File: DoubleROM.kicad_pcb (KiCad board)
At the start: 2 copper layers, 81.3 x 53.6 mm, 19 parts, among them J1 Bus_ISA_8bit, SW1 ROM 1 Config, SW2 ROM 2 Config, SW3 Size, SW4 Size, U1 ROM 1, U2 ROM 2, U3 74LS688, U4 74LS688, U5 74LS33

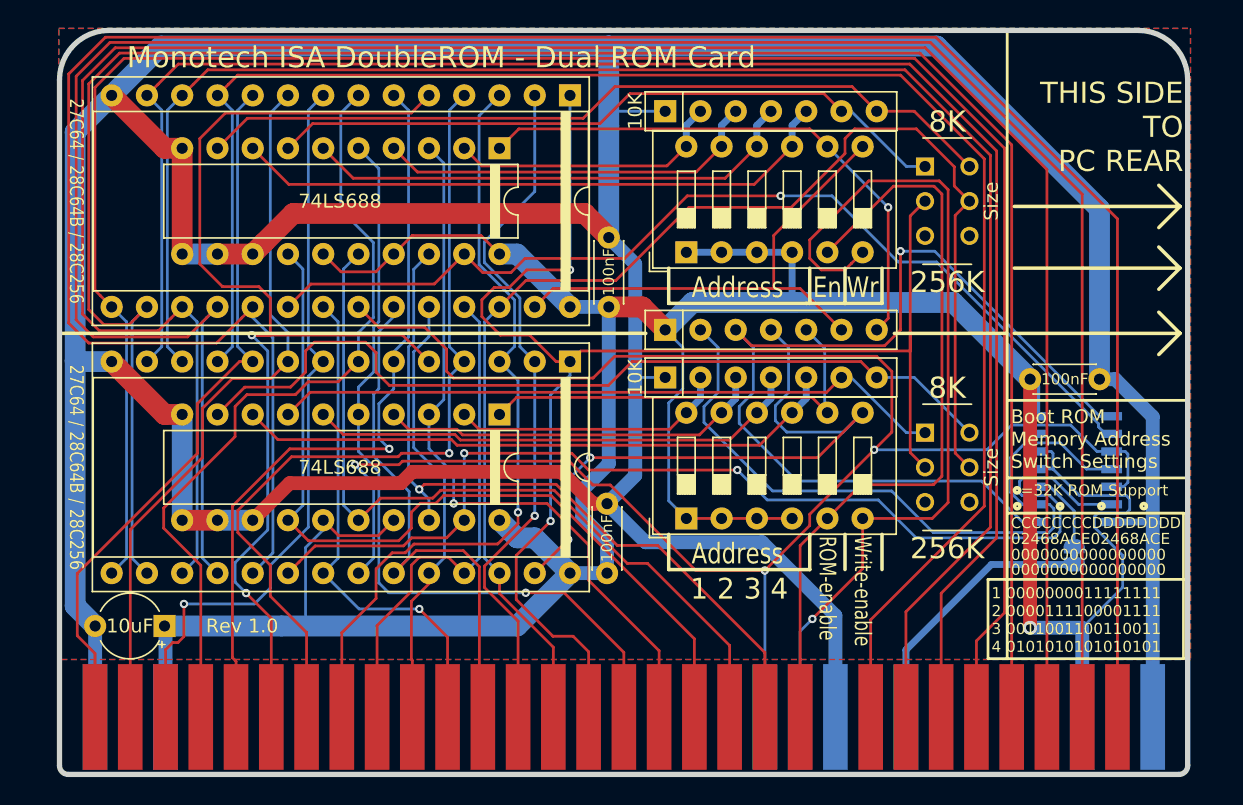
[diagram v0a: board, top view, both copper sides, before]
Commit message: minor change in text 256K to 32K
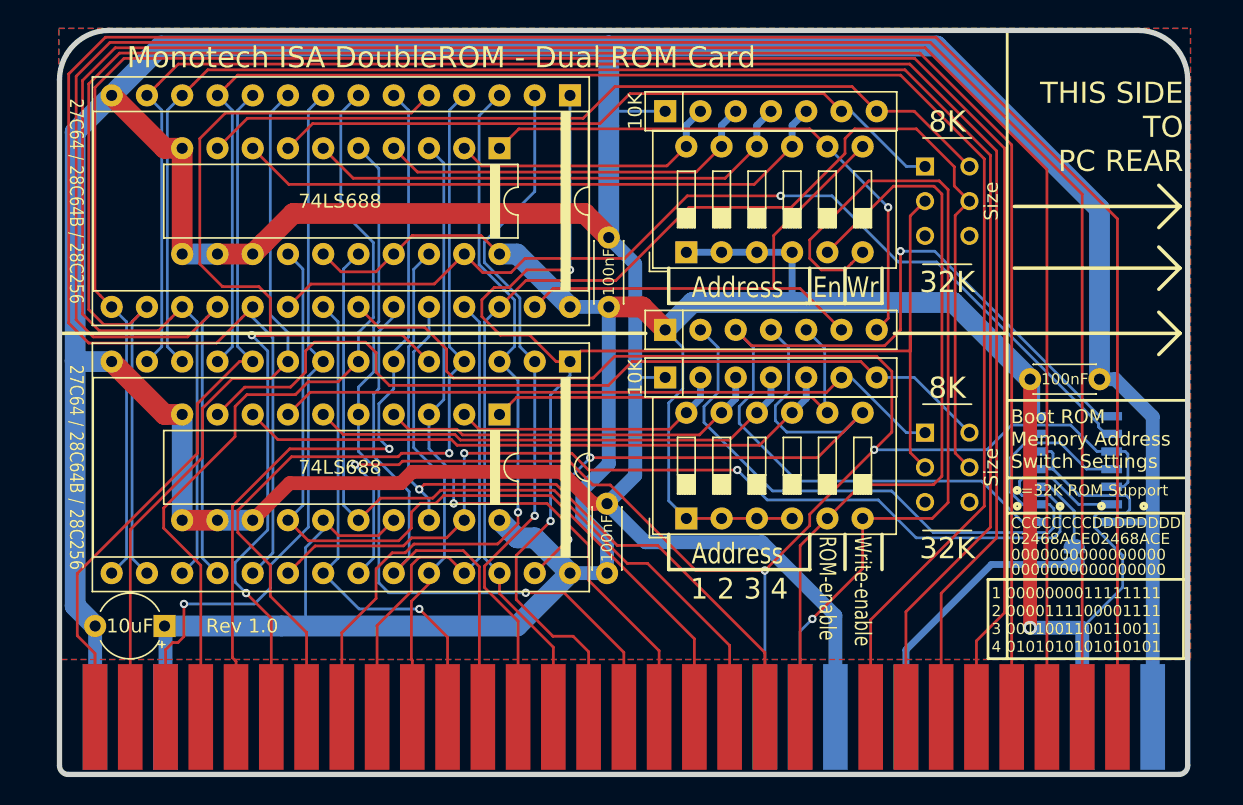
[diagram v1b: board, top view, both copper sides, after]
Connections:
- net /~MEMR renamed /~{MEMR}
- net /~MEMW renamed /~{MEMW}
- net /~ROMCS1 renamed /~{ROMCS1}
- net /~ROMCS2 renamed /~{ROMCS2}
- net /~ROMW1 renamed /~{ROMW1}
- net /~ROMW2 renamed /~{ROMW2}
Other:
- net class Default removed
- board text added: "32K"
- board text removed: "256K"
